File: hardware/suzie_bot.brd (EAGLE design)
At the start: 98.7 x 71.1 mm, 24 parts, among them IC1 LT1529CT33, IC2 L9637DDIP-ADAPTED, Y1 14.7456, Y2 6.0

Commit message: Updating board and schematic.
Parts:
- moved C4 1.91 mm to (54.0, 48.9), turned to 180 degrees
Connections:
- removed net N$11: U$1.D6, U$4.OFF
- removed net N$34: IC1.4, U$1.D5
- new net N$10: U$1.A6, U$4.OFF
- new net N$9: IC1.4, U$1.A7
- net CS-KLINE: now also U$1.A5; no longer U$1.A1
- net N$30: now also U$1.A4; no longer U$1.A7
- net N$33: now also U$1.D3; no longer U$1.A0
- net N$36: now also U$1.D8; no longer U$1.D4
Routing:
- net GND: track 250.1 -> 94.8 mm
- net 3V3: track 139.0 -> 186.8 mm
- net N$11: track 44.9 -> 0.00 mm
- net N$9: track 0.00 -> 36.3 mm
- net N$10: track 0.00 -> 26.5 mm
- net N$34: track 25.7 -> 0.00 mm
- net N$33: track 30.8 -> 9.79 mm
- net SCLK: track 123.4 -> 144.0 mm
- net N$25: track 34.3 -> 47.9 mm
- net MOSI: track 113.3 -> 125.7 mm
- net N$36: track 56.3 -> 44.7 mm
- net CS-KLINE: track 41.2 -> 31.3 mm
- net N$19: track 31.1 -> 40.1 mm
- net MISO: track 112.8 -> 118.8 mm
- net N$24: track 39.4 -> 44.7 mm, vias 1 -> 0
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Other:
- board text added: "suzibot 1.0"
- board text removed: "SUZIBOT 1.0"

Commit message: Updating board.
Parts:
- moved U$5 29.6 mm to (12.1, 44.5)
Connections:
- net N$33 renamed CS-GPSWIFI
- net GND: now also U$2.P$9, U$7.P$8
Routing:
- net GND: track 94.8 -> 103.7 mm
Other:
- board text added: "10 October 2016"
- board text added: "suzibot 1.1"
- board text removed: "8 October 2016"
- board text removed: "suzibot 1.0"
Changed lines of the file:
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@@
 <setting verticaltext="up"/>
 </settings>
-<grid distance="0.05" unitdist="inch" unit="inch" style="lines" multiple="1" display="no" altdistance="0.0125" altunitdist="inch" altunit="inch"/>
+<grid distance="0.05" unitdist="inch" unit="inch" style="lines" multiple="1" display="no" altdistance="0.0125" altunitdist="inch" altunit="mm"/>
 <layers>
 <layer number="1" name="Top" color="4" fill="1" visible="yes" active="yes"/>
@@
 <text x="97.79" y="53.34" size="1.016" layer="16" rot="MR270">L</text>
 <text x="97.79" y="69.85" size="1.016" layer="16" rot="MR270">GND</text>
-<text x="69.85" y="32.385" size="1.6764" layer="1" rot="SR270" align="bottom-right">suzibot
-1.0</text>
+<text x="69.85" y="32.385" size="1.6764" layer="21" rot="SR270" align="bottom-right">suzibot
+1.1</text>
 <text x="3.81" y="17.78" size="1.27" layer="16" rot="MR270">@coddingtonbear</text>
-<text x="6.985" y="16.51" size="1.27" layer="16" rot="MR270">8 October 2016</text>
+<text x="6.6675" y="17.145" size="1.27" layer="16" rot="MR270">10 October 2016</text>
 </plain>
 <attributes>
@@
 <element name="U$9" library="User-Submitted" package="LEVEL-SHIFTING-MICROSD" value="" x="74.295" y="24.765" rot="R180"/>
 <element name="U$10" library="voltage-sensor" package="VOLTAGE-SENSOR" value="VOLTAGE-SENSOR" x="92.71" y="26.67" rot="R180"/>
-<element name="U$5" library="featherwing" package="FEATHERWING" value="FEATHERWING" x="17.145" y="73.66" rot="R90"/>
+<element name="U$5" library="featherwing" package="FEATHERWING" value="FEATHERWING" x="12.065" y="44.45" rot="R90"/>
 <element name="U$11" library="tdk" package="17MM-PIEZO" value="PIEZO" x="15.24" y="9.525"/>
 <element name="U$2" library="nxp-semiconductors" package="TSSOP-28-ADAPTED" value="SC16IS752IPW" x="35.56" y="13.335" rot="R180"/>
@@
 <wire x1="66.04" y1="24.13" x2="65.405" y2="24.13" width="0.3048" layer="16"/>
 </signal>
-<signal name="N$33">
+<signal name="CS-GPSWIFI">
 <contactref element="U$2" pad="P$10"/>
+<wire x1="40.64" y1="26.035" x2="49.53" y2="26.035" width="0.3048" layer="16"/>
 <contactref element="U$1" pad="D3"/>
-<wire x1="40.64" y1="26.035" x2="49.53" y2="26.035" width="0.3048" layer="16"/>
 <wire x1="49.53" y1="26.035" x2="50.165" y2="26.67" width="0.3048" layer="16"/>
 </signal>
@@
 <contactref element="U$6" pad="P$4"/>
 <contactref element="U$6" pad="P$9"/>
-<polygon width="0.4064" layer="16" orphans="yes">
+<polygon width="0.4064" layer="16" isolate="0.4064" orphans="yes">
 <vertex x="0" y="71.12"/>
 <vertex x="99.06" y="71.12"/>
@@
 <wire x1="85.4075" y1="28.8925" x2="73.3425" y2="28.8925" width="0.4064" layer="1"/>
 <wire x1="73.3425" y1="28.8925" x2="69.215" y2="24.765" width="0.4064" layer="1"/>
+<contactref element="U$7" pad="P$8"/>
+<contactref element="U$2" pad="P$9"/>
+<wire x1="68.58" y1="52.705" x2="69.215" y2="52.705" width="0.3048" layer="16"/>
+<wire x1="69.215" y1="52.705" x2="70.485" y2="51.435" width="0.3048" layer="16"/>
+<wire x1="70.485" y1="51.435" x2="70.485" y2="45.4025" width="0.3048" layer="16"/>
+<wire x1="70.485" y1="45.4025" x2="70.1675" y2="45.085" width="0.3048" layer="16"/>
 </signal>
 <signal name="3V3" class="1">

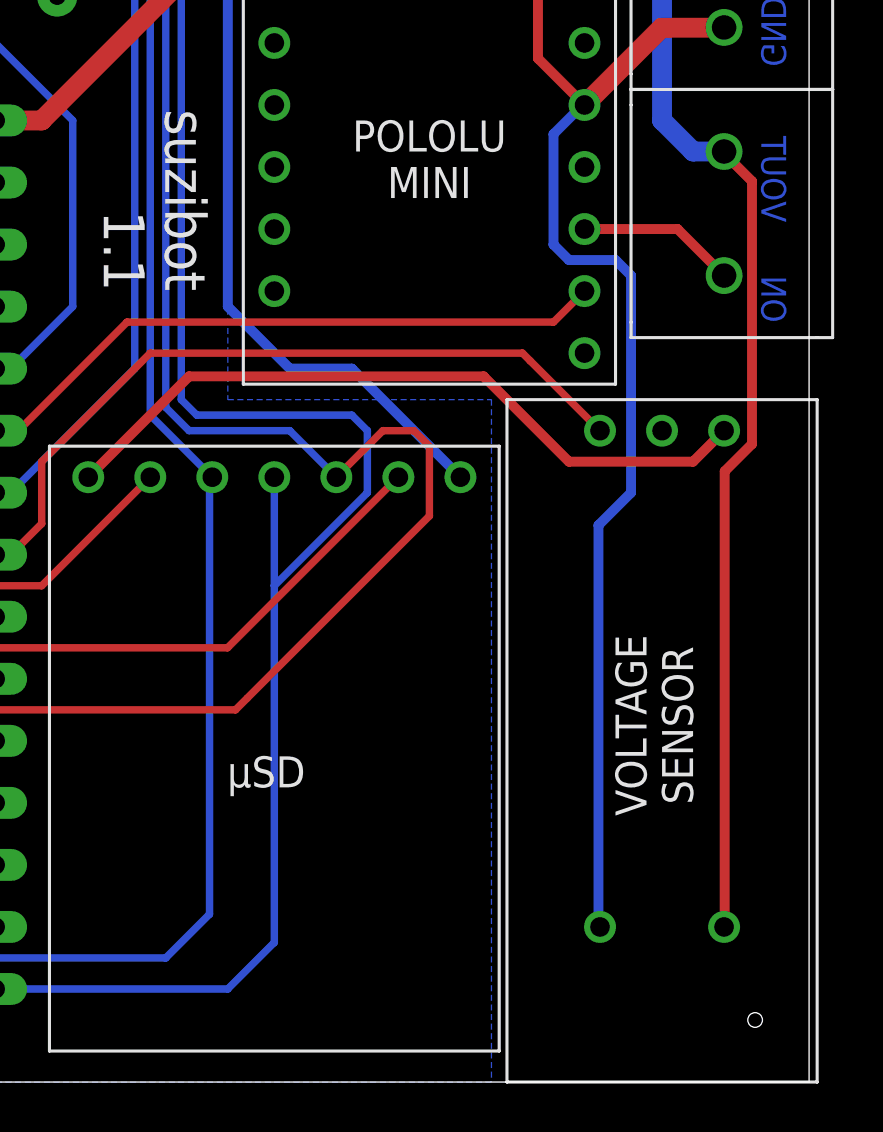
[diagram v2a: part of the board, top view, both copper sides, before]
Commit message: Moving voltage sensor slightly closer to edge.
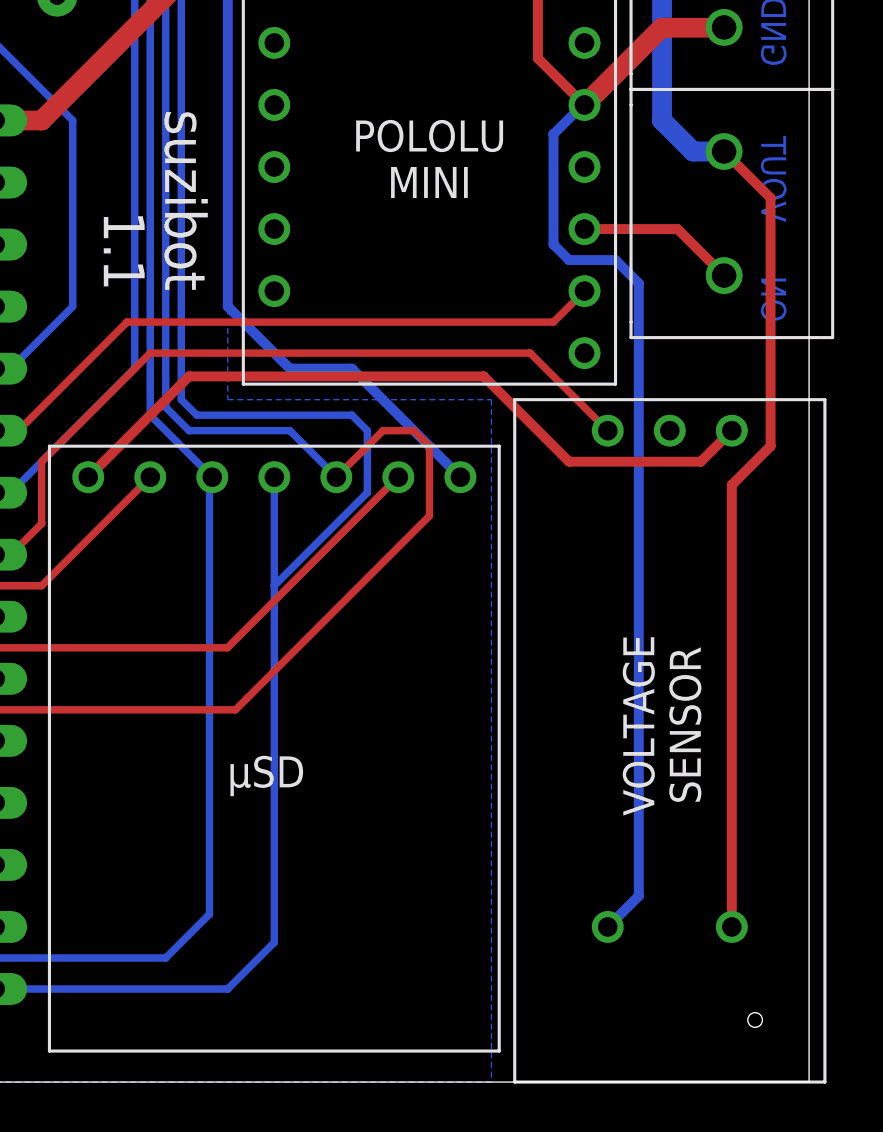
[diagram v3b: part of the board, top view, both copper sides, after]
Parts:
- moved U$10 0.32 mm to (93.0, 26.7)
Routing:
- net 12V-OUT: track 69.9 -> 70.4 mm
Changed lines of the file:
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@@
 <element name="U$7" library="nxp-semiconductors" package="TSSOP-24-ADAPTED" value="SC16IS750IPWDIP-24" x="66.04" y="60.325" rot="R90"/>
 <element name="U$9" library="User-Submitted" package="LEVEL-SHIFTING-MICROSD" value="" x="74.295" y="24.765" rot="R180"/>
-<element name="U$10" library="voltage-sensor" package="VOLTAGE-SENSOR" value="VOLTAGE-SENSOR" x="92.71" y="26.67" rot="R180"/>
+<element name="U$10" library="voltage-sensor" package="VOLTAGE-SENSOR" value="VOLTAGE-SENSOR" x="93.0275" y="26.67" rot="R180"/>
 <element name="U$5" library="featherwing" package="FEATHERWING" value="FEATHERWING" x="12.065" y="44.45" rot="R90"/>
 <element name="U$11" library="tdk" package="17MM-PIEZO" value="PIEZO" x="15.24" y="9.525"/>
@@
 <signal name="N$30">
 <contactref element="U$10" pad="S"/>
-<wire x1="90.17" y1="26.67" x2="87.3125" y2="29.5275" width="0.3048" layer="1"/>
 <contactref element="U$1" pad="A4"/>
 <wire x1="65.405" y1="21.59" x2="66.04" y2="21.59" width="0.3048" layer="1"/>
@@
 <wire x1="67.31" y1="22.86" x2="67.31" y2="25.4" width="0.3048" layer="1"/>
 <wire x1="67.31" y1="25.4" x2="71.755" y2="29.845" width="0.3048" layer="1"/>
-<wire x1="71.755" y1="29.845" x2="86.995" y2="29.845" width="0.3048" layer="1"/>
-<wire x1="86.995" y1="29.845" x2="87.3125" y2="29.5275" width="0.3048" layer="1"/>
+<wire x1="71.755" y1="29.845" x2="87.3125" y2="29.845" width="0.3048" layer="1"/>
+<wire x1="87.3125" y1="29.845" x2="90.4875" y2="26.67" width="0.3048" layer="1"/>
 </signal>
 <signal name="N$36">
@@
 <contactref element="IC2" pad="VS"/>
 <contactref element="ON/12V-OUT" pad="P$2"/>
-<wire x1="95.2754" y1="25.0063" x2="95.2754" y2="6.4262" width="0.4064" layer="1"/>
-<wire x1="96.393" y1="26.1239" x2="95.2754" y2="25.0063" width="0.4064" layer="1"/>
-<wire x1="96.393" y1="36.8808" x2="96.393" y2="26.1239" width="0.4064" layer="1"/>
-<wire x1="95.2754" y1="37.9984" x2="96.393" y2="36.8808" width="0.4064" layer="1"/>
-<wire x1="95.2754" y1="6.4262" x2="95.25" y2="6.35" width="0.4064" layer="1"/>
-<wire x1="95.2754" y1="37.9984" x2="95.25" y2="38.1" width="0.4064" layer="1"/>
 <wire x1="95.25" y1="38.1" x2="93.98" y2="38.1" width="0.8128" layer="16"/>
 <wire x1="93.98" y1="38.1" x2="92.71" y2="39.37" width="0.8128" layer="16"/>
@@
 <wire x1="89.535" y1="56.515" x2="86.36" y2="53.34" width="0.3048" layer="16"/>
 <wire x1="86.36" y1="53.34" x2="86.36" y2="48.26" width="0.3048" layer="16"/>
+<wire x1="95.5675" y1="6.35" x2="95.5675" y2="24.4475" width="0.4064" layer="1"/>
+<wire x1="95.5675" y1="24.4475" x2="97.155" y2="26.035" width="0.4064" layer="1"/>
+<wire x1="97.155" y1="26.035" x2="97.155" y2="36.195" width="0.4064" layer="1"/>
+<wire x1="97.155" y1="36.195" x2="95.25" y2="38.1" width="0.4064" layer="1"/>
 </signal>
 <signal name="POWERON" class="1">
@@
 <wire x1="95.1357" y1="43.1673" x2="95.25" y2="43.18" width="0.4064" layer="1"/>
 <wire x1="89.408" y1="39.9542" x2="88.265" y2="38.8112" width="0.4064" layer="16"/>
-<wire x1="90.1065" y1="6.4262" x2="90.17" y2="6.35" width="0.4064" layer="16"/>
 <wire x1="89.408" y1="39.9542" x2="89.535" y2="40.005" width="0.4064" layer="16"/>
-<wire x1="90.1065" y1="6.4262" x2="90.1065" y2="22.7965" width="0.4064" layer="16"/>
-<wire x1="90.1065" y1="22.7965" x2="91.44" y2="24.13" width="0.4064" layer="16"/>
-<wire x1="91.44" y1="24.13" x2="91.44" y2="33.02" width="0.4064" layer="16"/>
-<wire x1="91.44" y1="33.02" x2="90.805" y2="33.655" width="0.4064" layer="16"/>
 <wire x1="90.805" y1="33.655" x2="88.9" y2="33.655" width="0.4064" layer="16"/>
 <wire x1="88.9" y1="33.655" x2="88.265" y2="34.29" width="0.4064" layer="16"/>
@@
 <wire x1="95.1357" y1="43.1673" x2="92.6973" y2="43.1673" width="0.8128" layer="1"/>
 <wire x1="92.6973" y1="43.1673" x2="89.535" y2="40.005" width="0.8128" layer="1"/>
+<wire x1="90.805" y1="33.655" x2="91.7575" y2="32.7025" width="0.4064" layer="16"/>
+<wire x1="91.7575" y1="32.7025" x2="91.7575" y2="7.62" width="0.4064" layer="16"/>
+<wire x1="91.7575" y1="7.62" x2="90.4875" y2="6.35" width="0.4064" layer="16"/>
 </signal>
 <signal name="GND" class="1">
@@
 <wire x1="93.98" y1="67.31" x2="95.25" y2="67.31" width="0.4064" layer="16"/>
 <wire x1="95.25" y1="68.58" x2="95.25" y2="67.31" width="0.4064" layer="16"/>
-<wire x1="95.25" y1="26.67" x2="93.98" y2="25.4" width="0.4064" layer="1"/>
-<wire x1="93.98" y1="25.4" x2="88.9" y2="25.4" width="0.4064" layer="1"/>
 <wire x1="88.9" y1="25.4" x2="85.4075" y2="28.8925" width="0.4064" layer="1"/>
 <wire x1="85.4075" y1="28.8925" x2="73.3425" y2="28.8925" width="0.4064" layer="1"/>
@@
 <wire x1="70.485" y1="51.435" x2="70.485" y2="45.4025" width="0.3048" layer="16"/>
 <wire x1="70.485" y1="45.4025" x2="70.1675" y2="45.085" width="0.3048" layer="16"/>
+<wire x1="88.9" y1="25.4" x2="94.2975" y2="25.4" width="0.4064" layer="1"/>
+<wire x1="94.2975" y1="25.4" x2="95.5675" y2="26.67" width="0.4064" layer="1"/>
 </signal>
 <signal name="3V3" class="1">
